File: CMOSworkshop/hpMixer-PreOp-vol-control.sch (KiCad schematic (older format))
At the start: 24 parts, among them U4 TL082

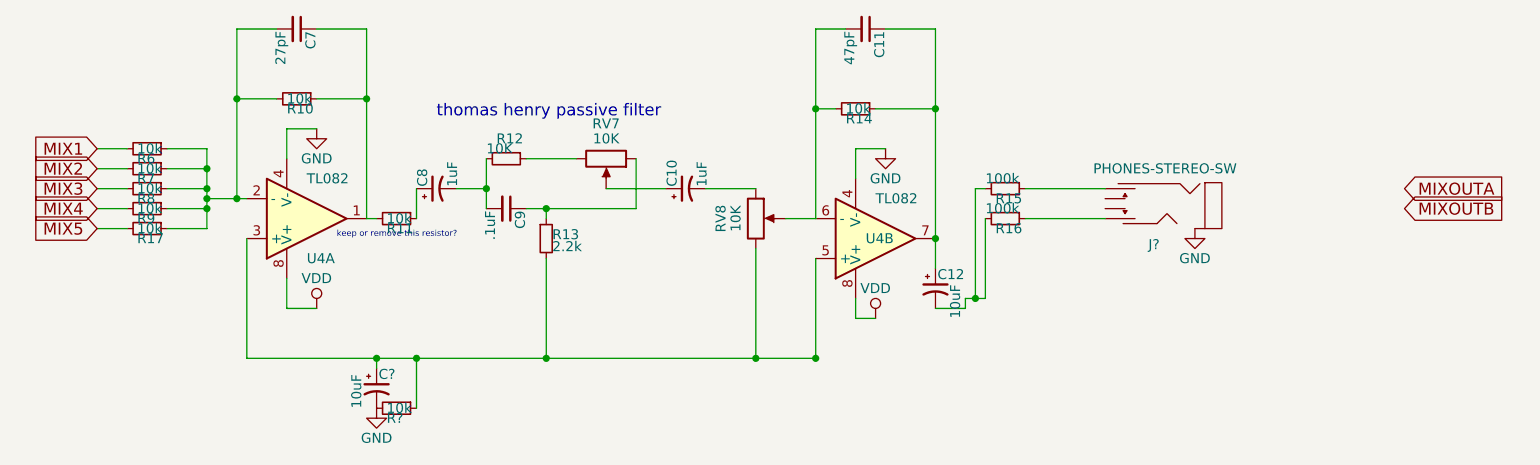
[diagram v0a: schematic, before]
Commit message: updated mixer schematic, added 9v battery holder and laid out components.
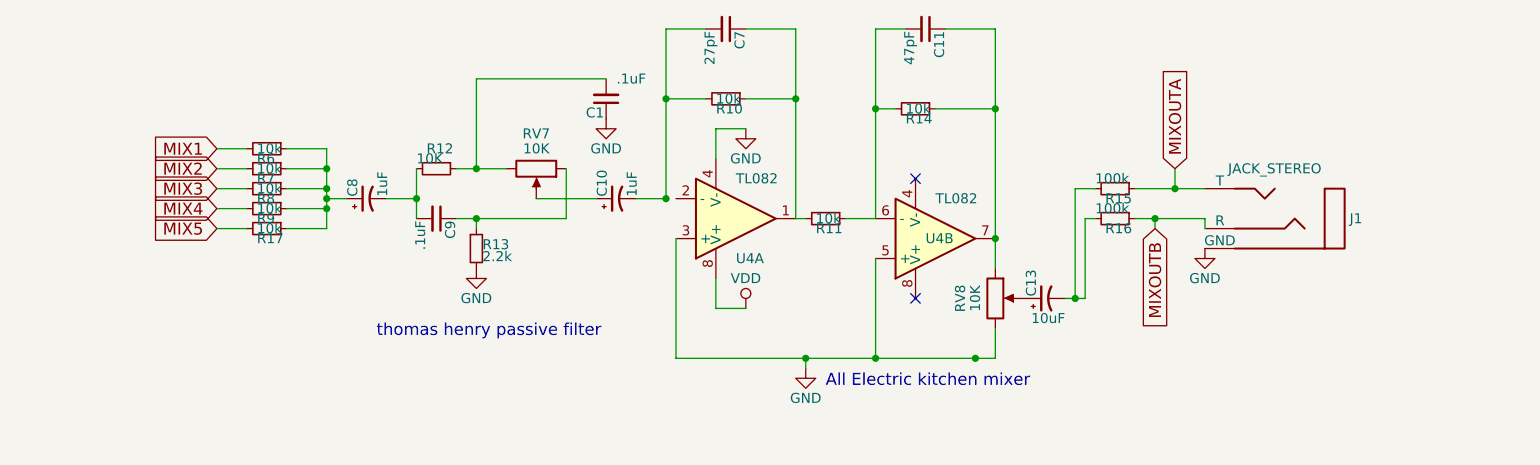
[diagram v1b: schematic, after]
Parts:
- removed C12, C?: 10uF, Capacitors_THT:CP_Radial_D5.0mm_P2.50mm, symbol CP1_Small
- removed J?: PHONES-STEREO-SW, symbol PHONES-STEREO-SW
- removed R?: 10k, 4ms-footprints:R-TH, symbol R_Small
- added C1: .1uF, Capacitors_THT:CP_Radial_D5.0mm_P2.50mm, symbol C_Small
- added C13: 10uF, Capacitors_THT:CP_Radial_D5.0mm_P2.50mm, symbol CP1_Small
- added J1: JACK_STEREO, malekko main:J355W, symbol JACK_STEREO
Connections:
- net GND: now also R13.2, RV8.3, U4.3 (+), U4.5 (+), C1.1, J1.1 (GND); no longer U4.4 (V-)
- net MIXOUTA: now also R15.1, J1.2 (T)
- net MIXOUTB: now also R16.1, J1.3 (R)
- net VDD: no longer U4.8 (V+)
- net at R17.1, R6.1, R7.1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: now also C8.+; no longer C7.2, R10.2, U4.2 (-)
- net at C11.2, R14.2, U4.6 (-): now also R11.1; no longer RV8.2
- net at C11.1, R14.1, U4.7: now also RV8.1
- net at C10.-: now also C7.2, R10.2; no longer RV8.1
- net at R15.2, R16.2: now also C13.-
- net at R12.1, RV7.3: now also C1.2
- new net: C13.+, RV8.2
- no-connect marks 0 -> 2
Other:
- note added: "All Electric kitchen mixer\n"
- note removed: "keep or remove this resistor?\n"
- moved on the sheet: C10, C11, C7, C8, C9, R10, R11, R12, R13, R14, R15, R16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
